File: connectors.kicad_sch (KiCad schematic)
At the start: 0 parts

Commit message: [#103224] Add JTAG connector, add 2nd QSPI flash in co-layout, add Antmicro and OSH logos
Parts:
- added C7001: C_10u_10V_X7R_0603, antmicro-footprints:C_0603_1608Metric, symbol Antmicro Symbols:C_10u_10V_X7R_0603
- added J7001: PinHeader_2x10_P2.54mm_SMD_SHF-110-01-L-D-SM-TR, antmicro-footprints:PinHeader_2x10_P2.54mm_SMD_SHF-110-01-L-D-SM-TR, symbol Antmicro Symbols:PinHeader_2x10_P2.54mm_SMD_SHF-110-01-L-D-SM-TR
- added R7001, R7002, R7003, R7004: R_10k_0402, antmicro-footprints:R_0402_1005Metric, symbol Antmicro Symbols:R_10k_0402
- added R7005: R_100k_0402, antmicro-footprints:R_0402_1005Metric, symbol Antmicro Symbols:R_100k_0402
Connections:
- new net +3V3: J7001.1, R7001.2, R7002.2, R7003.2, R7004.2, R7005.2
- new net EC_JTAG_TCK: J7001.9, R7003.1
- new net EC_JTAG_TDI: J7001.5, R7001.1
- new net EC_JTAG_TDO: J7001.13, R7004.1
- new net EC_JTAG_TMS: J7001.7, R7002.1
- new net EC_JTAG_nRST: C7001.2, R7005.1
- new net GND: C7001.1, J7001.10, J7001.11, J7001.12, J7001.18, J7001.20, J7001.4, J7001.6, J7001.8
- no-connect marks 0 -> 7
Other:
- note added: "JTAG"

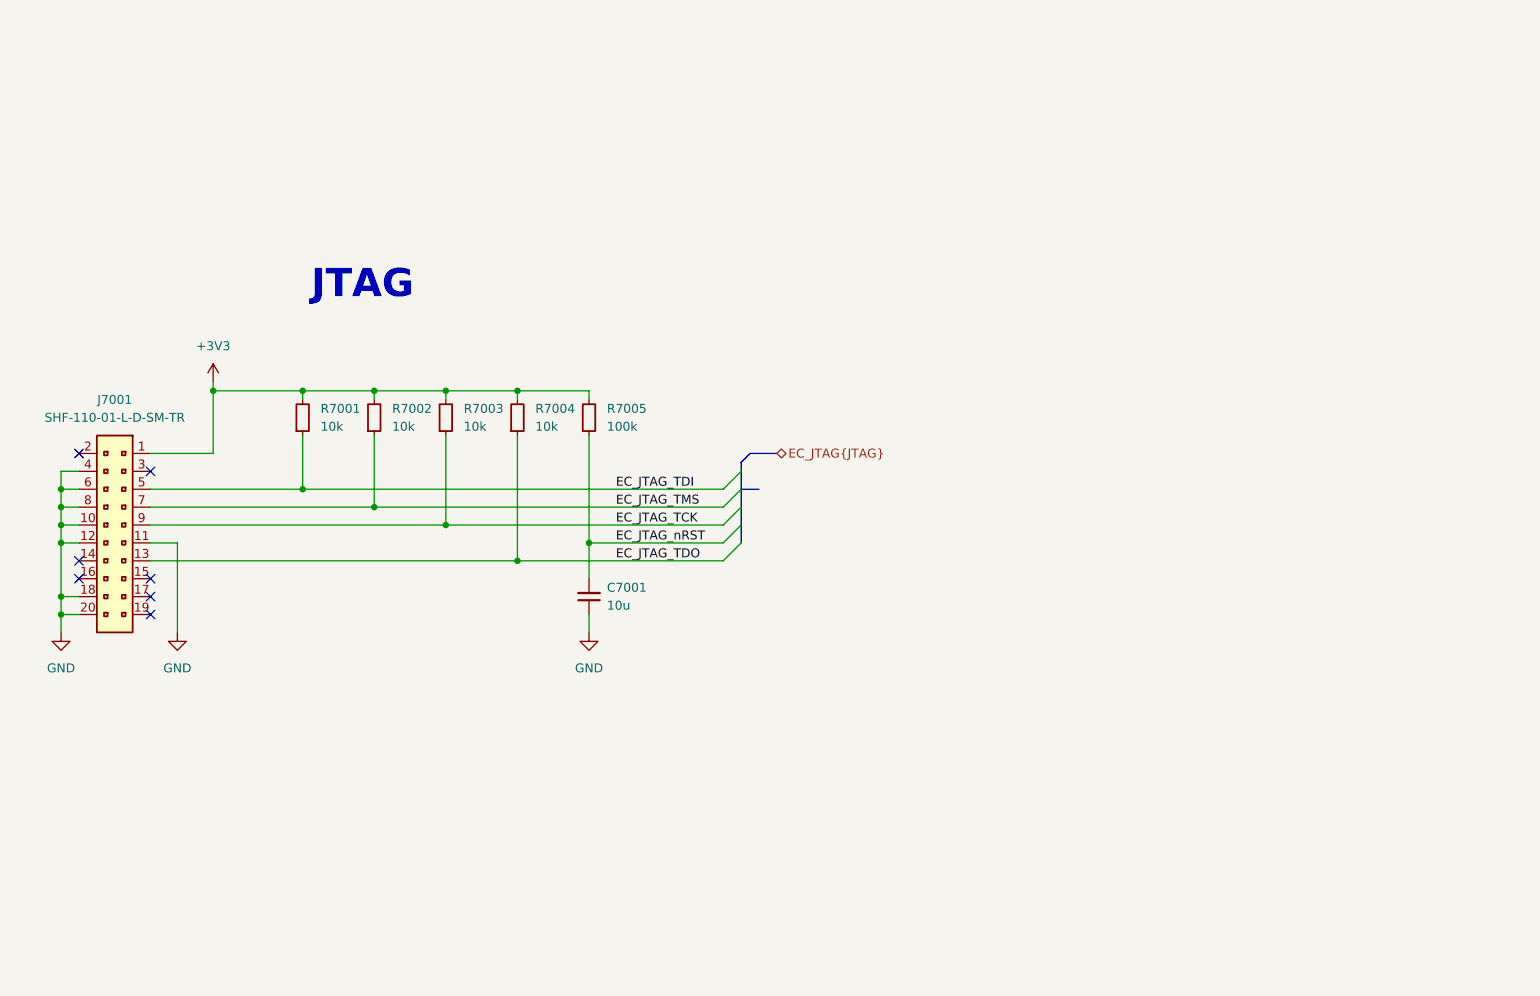
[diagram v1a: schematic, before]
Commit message: [#103224] Add MEC1723 IC, JTAG connections, eSPI connections, QSPI connections, fix typo in UART
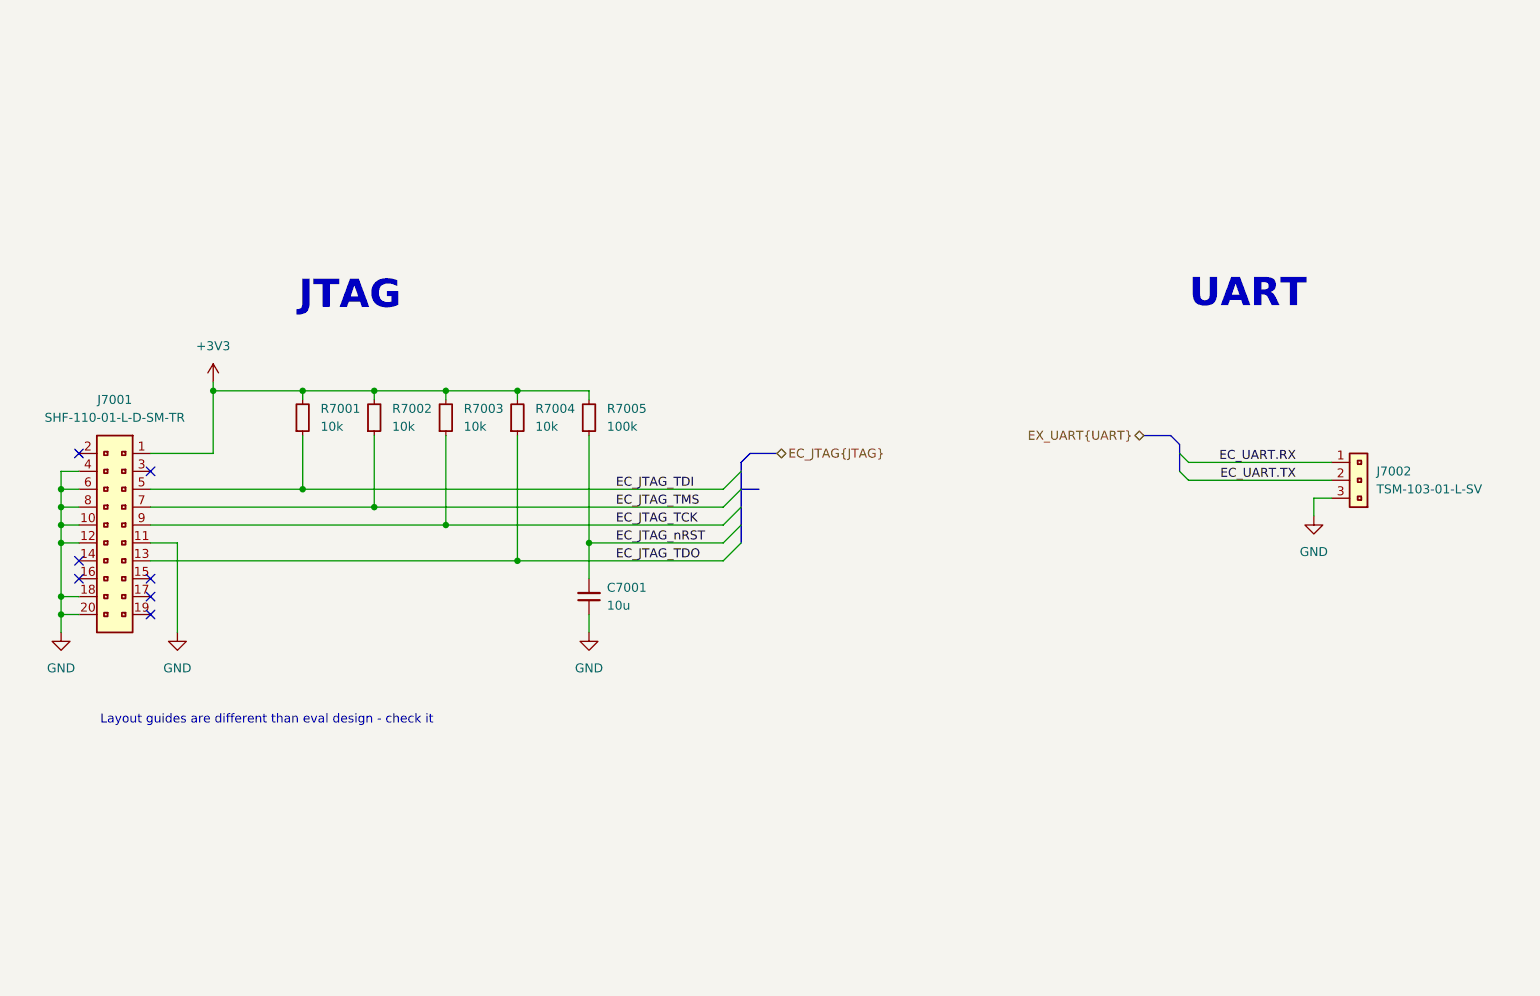
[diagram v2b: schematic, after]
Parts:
- added J7002: PinHeader_1x3_P2.54mm_SMD, antmicro-footprints:PinHeader_1x3_P2.54mm_SMD, symbol Antmicro Symbols:PinHeader_1x3_P2.54mm_SMD
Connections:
- net GND: now also J7002.3
- new net EC_UART.RX: J7002.1
- new net EC_UART.TX: J7002.2
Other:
- note added: "Layout guides are different than eval design - check it"
- note added: "UART"

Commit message: [#103224] Change buffer ICs, change JTAG connector, move BSS_STRAP resistors to MEC1723 sheet
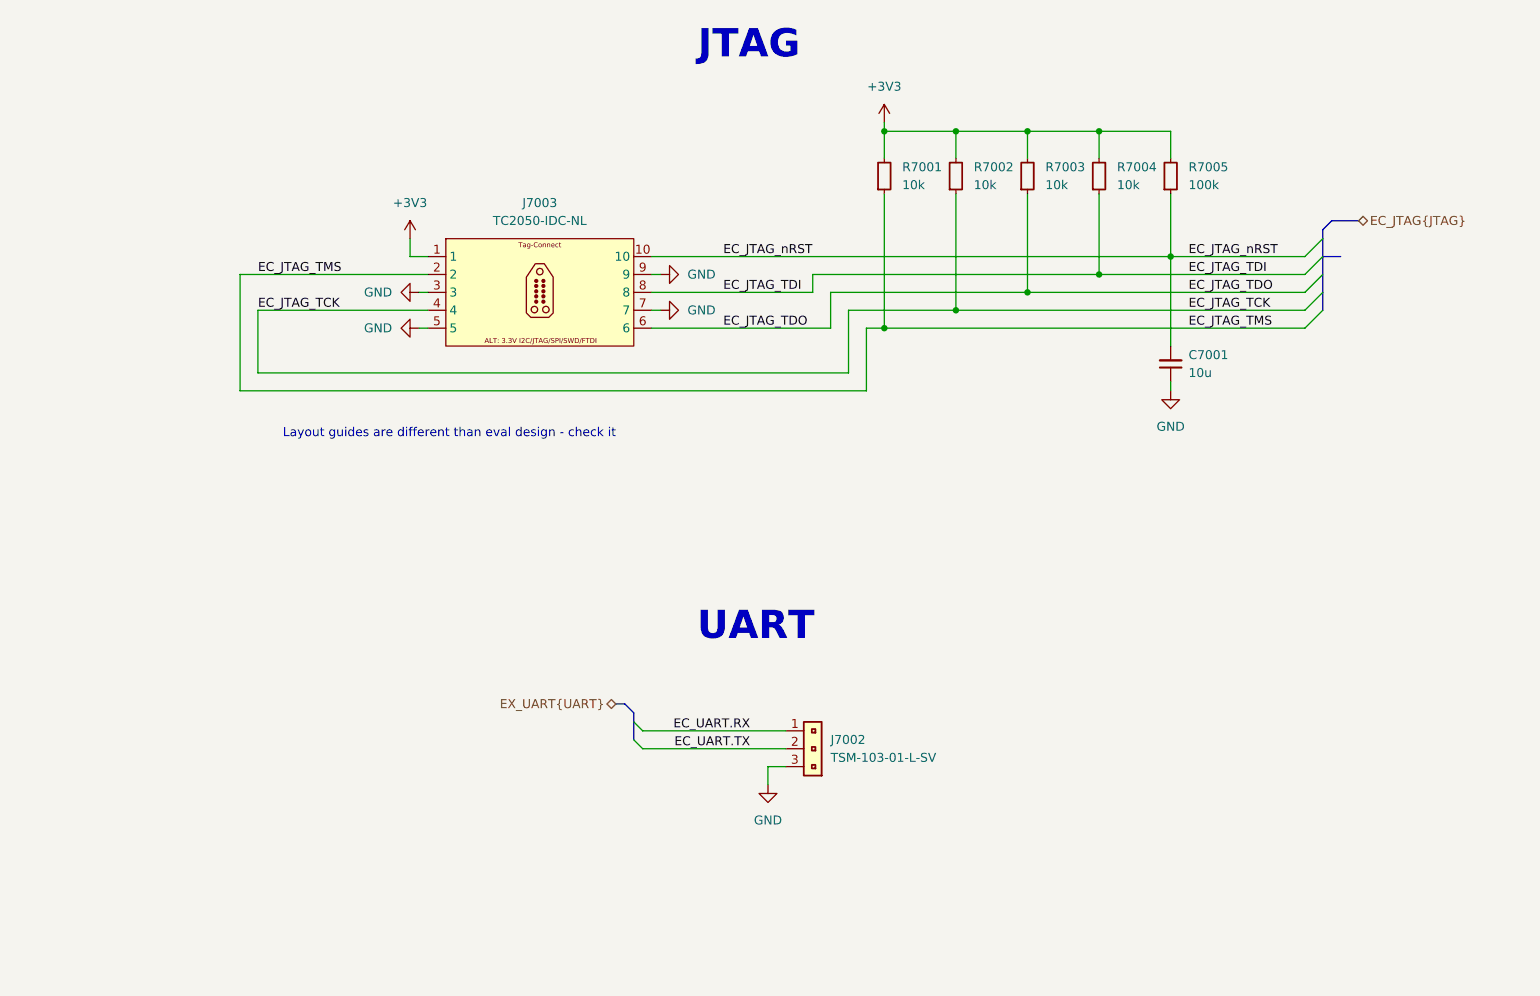
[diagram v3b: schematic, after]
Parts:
- removed J7001: PinHeader_2x10_P2.54mm_SMD_SHF-110-01-L-D-SM-TR, antmicro-footprints:PinHeader_2x10_P2.54mm_SMD_SHF-110-01-L-D-SM-TR, symbol Antmicro Symbols:PinHeader_2x10_P2.54mm_SMD_SHF-110-01-L-D-SM-TR
- added J7003: Tag-Connect_TC2050-IDC-NL_2x5_P1.27mm, antmicro-footprints:Tag-Connect_TC2050-IDC-NL_2x5_P1.27mm, symbol Antmicro Symbols:Tag-Connect_TC2050-IDC-NL_2x5_P1.27mm
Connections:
- net +3V3: now also J7003.1
- net EC_JTAG_TCK: now also R7002.1, J7003.4; no longer R7003.1
- net EC_JTAG_TDI: now also R7004.1, J7003.8; no longer R7001.1
- net EC_JTAG_TDO: now also R7003.1, J7003.6; no longer R7004.1
- net EC_JTAG_TMS: now also R7001.1, J7003.2; no longer R7002.1
- net EC_JTAG_nRST: now also J7003.10
- net GND: now also J7003.3, J7003.5, J7003.7, J7003.9
- no-connect marks 7 -> 0
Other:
- moved on the sheet: C7001, J7002, R7001, R7002, R7003, R7004, R7005

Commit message: [#103224] Divide 7SEG bus into 2, rename JTAG connector pins
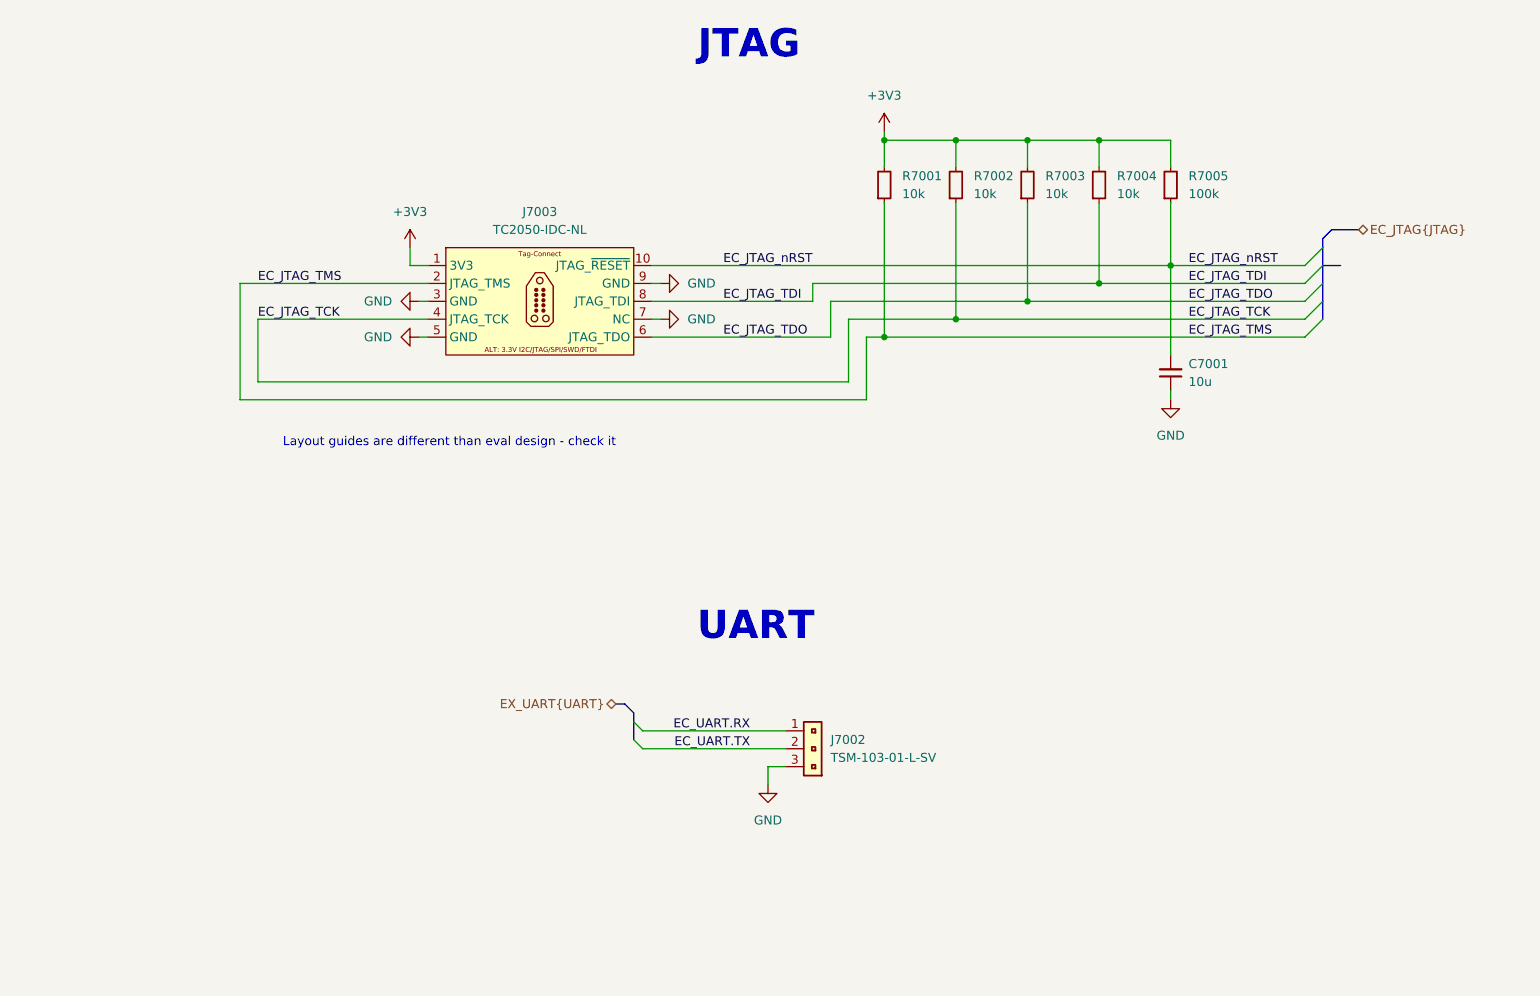
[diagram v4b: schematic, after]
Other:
- moved on the sheet: C7001, J7003, R7001, R7002, R7003, R7004, R7005

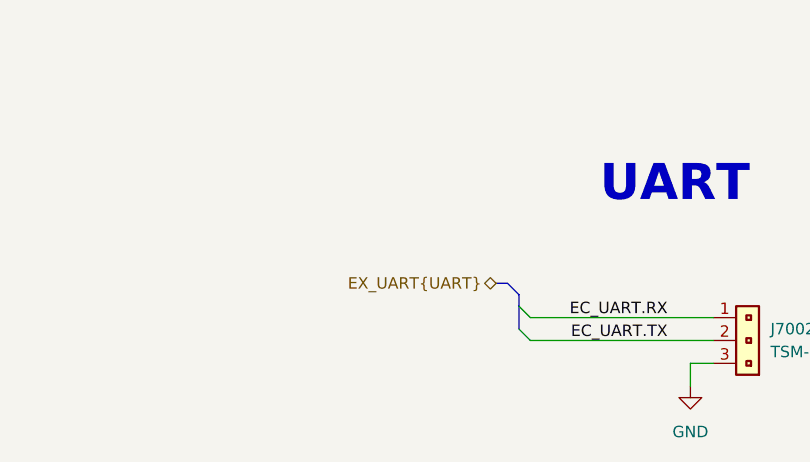
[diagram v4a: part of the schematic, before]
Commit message: [#103224] Add root schematic connections, add EMDRST button, add 1u decoupling capacitors, connect UART, add fiducials
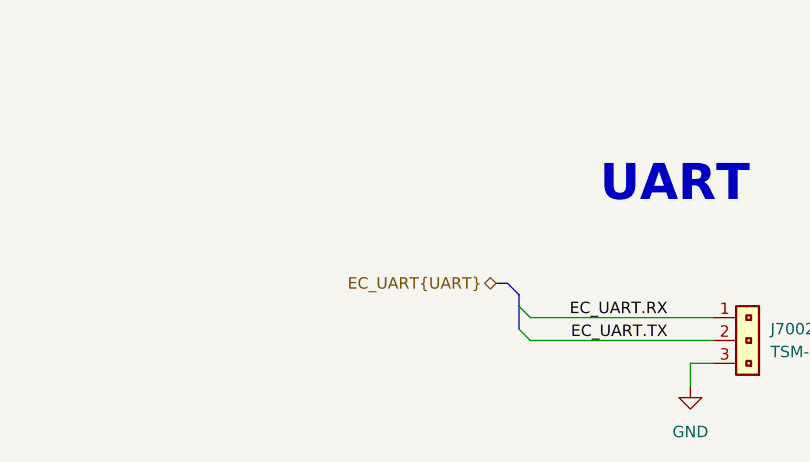
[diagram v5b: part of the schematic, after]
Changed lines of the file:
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@@
 		)
 	)
-	(hierarchical_label "EX_UART{UART}"
+	(hierarchical_label "EC_UART{UART}"
 		(shape bidirectional)
 		(at 124.46 118.11 180)

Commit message: [#103224] Add UART1, added GND to breakout connectors, fix orientation of DC-SCM connector, delete unused notes
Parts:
- added J7001: PinHeader_1x3_P2.54mm_SMD, antmicro-footprints:PinHeader_1x3_P2.54mm_SMD, symbol Antmicro Symbols:PinHeader_1x3_P2.54mm_SMD
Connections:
- net GND: now also J7001.3
- net EC_UART.RX renamed EC_UART0.RX
- net EC_UART.TX renamed EC_UART0.TX
- new net EC_UART1.RX: J7001.1
- new net EC_UART1.TX: J7001.2

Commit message: chore: set date and project name
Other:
- company: (none) -> Antmicro
- title: (none) -> eSPI Adapter
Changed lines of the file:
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@@
 	(generator_version "10.0")
 	(paper "A4")
+	(title_block
+		(title "eSPI Adapter")
+		(date "2026-08-21")
+		(rev "1.0.0")
+		(company "Antmicro")
+	)
 	(text "UART"
 		(exclude_from_sim no)
